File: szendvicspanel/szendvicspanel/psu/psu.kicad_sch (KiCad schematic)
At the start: 7 parts

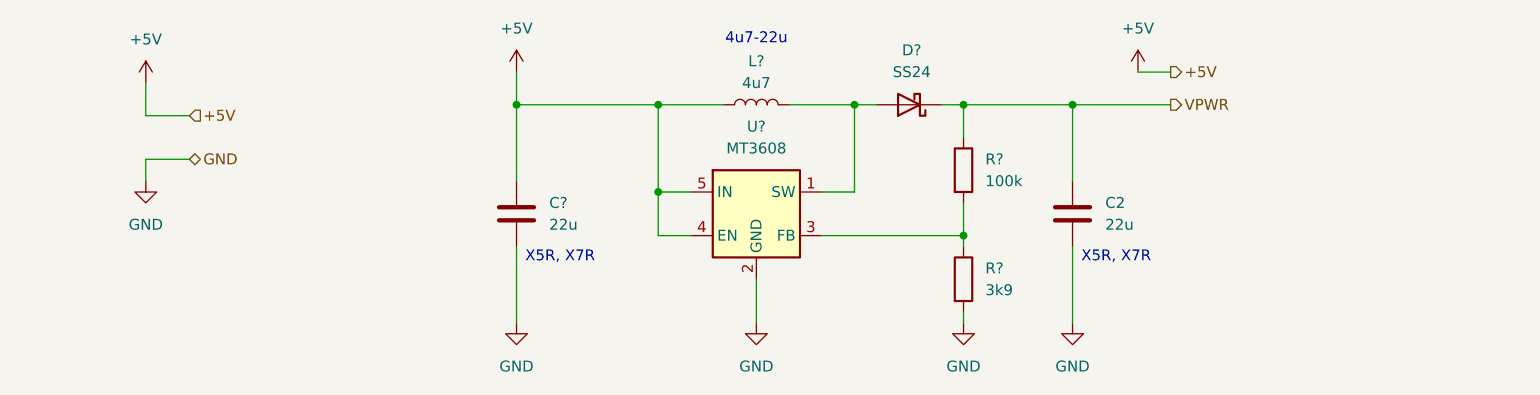
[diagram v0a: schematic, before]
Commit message: Átstrukturálás hierarchikus PCB-hez
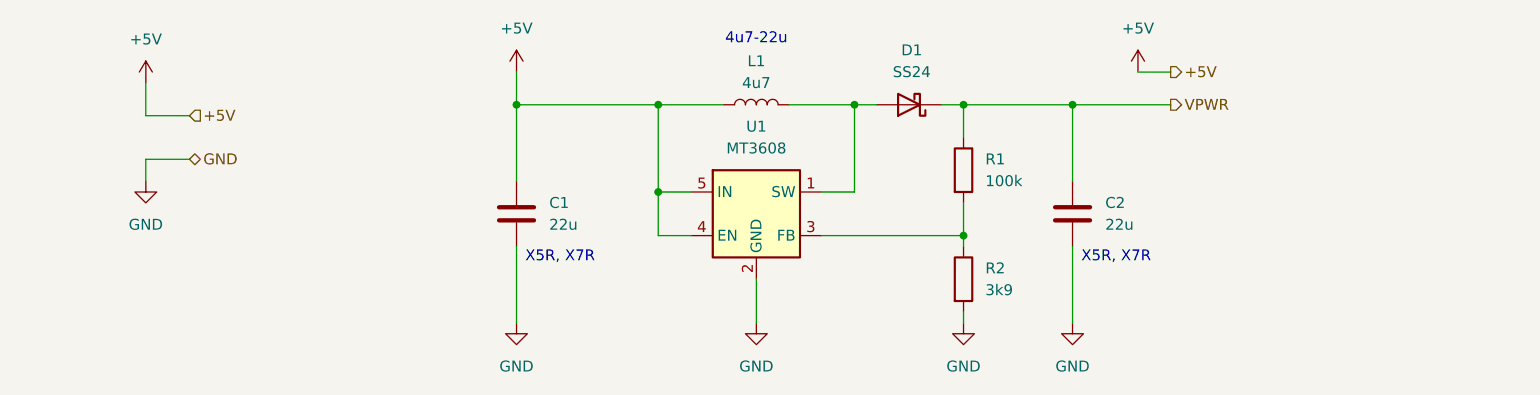
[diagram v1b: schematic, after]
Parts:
- gave numbers to parts that had none: 6
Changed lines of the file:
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@@
 		(dnp no)
 		(fields_autoplaced yes)
-		(property "Reference" "D?"
+		(property "Reference" "D1"
 			(at 167.9575 81.28 0)
 			(effects
@@
 			(project "szendvicspanel"
 				(path "/2e536be4-7a69-4064-ab31-c73232c2dcfe/c1a87f4a-0473-4080-9ef3-9f191c8d170d"
-					(reference "D?")
+					(reference "D1")
 					(unit 1)
 				)
@@
 		(dnp no)
 		(fields_autoplaced yes)
-		(property "Reference" "#PWR?"
+		(property "Reference" "#PWR07"
 			(at 121.92 119.38 0)
 			(effects
@@
 			(project "szendvicspanel"
 				(path "/2e536be4-7a69-4064-ab31-c73232c2dcfe/c1a87f4a-0473-4080-9ef3-9f191c8d170d"
-					(reference "#PWR?")
+					(reference "#PWR07")
 					(unit 1)
 				)
@@
 		(dnp no)
 		(fields_autoplaced yes)
-		(property "Reference" "#PWR015"
+		(property "Reference" "#PWR04"
 			(at 78.74 88.9 0)
 			(effects
@@
 			(project ""
 				(path "/2e536be4-7a69-4064-ab31-c73232c2dcfe/c1a87f4a-0473-4080-9ef3-9f191c8d170d"
-					(reference "#PWR015")
+					(reference "#PWR04")
 					(unit 1)
 				)
@@
 		(dnp no)
 		(fields_autoplaced yes)
-		(property "Reference" "U?"
+		(property "Reference" "U1"
 			(at 149.86 90.17 0)
 			(effects
@@
 			(project "szendvicspanel"
 				(path "/2e536be4-7a69-4064-ab31-c73232c2dcfe/c1a87f4a-0473-4080-9ef3-9f191c8d170d"
-					(reference "U?")
+					(reference "U1")
 					(unit 1)
 				)
@@
 		(dnp no)
 		(fields_autoplaced yes)
-		(property "Reference" "R?"
+		(property "Reference" "R2"
 			(at 176.53 106.6799 0)
 			(effects
@@
 			(project "szendvicspanel"
 				(path "/2e536be4-7a69-4064-ab31-c73232c2dcfe/c1a87f4a-0473-4080-9ef3-9f191c8d170d"
-					(reference "R?")
+					(reference "R2")
 					(unit 1)
 				)
@@
 		(dnp no)
 		(fields_autoplaced yes)
-		(property "Reference" "#PWR?"
+		(property "Reference" "#PWR011"
 			(at 194.31 87.63 0)
 			(effects
@@
 			(project "szendvicspanel"
 				(path "/2e536be4-7a69-4064-ab31-c73232c2dcfe/c1a87f4a-0473-4080-9ef3-9f191c8d170d"
-					(reference "#PWR?")
+					(reference "#PWR011")
 					(unit 1)
 				)
@@
 		(dnp no)
 		(fields_autoplaced yes)
-		(property "Reference" "#PWR?"
+		(property "Reference" "#PWR06"
 			(at 121.92 87.63 0)
 			(effects
@@
 			(project "szendvicspanel"
 				(path "/2e536be4-7a69-4064-ab31-c73232c2dcfe/c1a87f4a-0473-4080-9ef3-9f191c8d170d"
-					(reference "#PWR?")
+					(reference "#PWR06")
 					(unit 1)
 				)
@@
 		(dnp no)
 		(fields_autoplaced yes)
-		(property "Reference" "#PWR?"
+		(property "Reference" "#PWR08"
 			(at 149.86 119.38 0)
 			(effects
@@
 			(project "szendvicspanel"
 				(path "/2e536be4-7a69-4064-ab31-c73232c2dcfe/c1a87f4a-0473-4080-9ef3-9f191c8d170d"
-					(reference "#PWR?")
+					(reference "#PWR08")
 					(unit 1)
 				)
@@
 		(dnp no)
 		(fields_autoplaced yes)
-		(property "Reference" "L?"
+		(property "Reference" "L1"
 			(at 149.86 82.55 90)
 			(effects
@@
 			(project "szendvicspanel"
 				(path "/2e536be4-7a69-4064-ab31-c73232c2dcfe/c1a87f4a-0473-4080-9ef3-9f191c8d170d"
-					(reference "L?")
+					(reference "L1")
 					(unit 1)
 				)
@@
 		(dnp no)
 		(fields_autoplaced yes)
-		(property "Reference" "#PWR?"
+		(property "Reference" "#PWR010"
 			(at 186.69 119.38 0)
 			(effects
@@
 			(project "szendvicspanel"
 				(path "/2e536be4-7a69-4064-ab31-c73232c2dcfe/c1a87f4a-0473-4080-9ef3-9f191c8d170d"
-					(reference "#PWR?")
+					(reference "#PWR010")
 					(unit 1)
 				)
@@
 		(dnp no)
 		(fields_autoplaced yes)
-		(property "Reference" "C?"
+		(property "Reference" "C1"
 			(at 125.73 99.0599 0)
 			(effects
@@
 			(project "szendvicspanel"
 				(path "/2e536be4-7a69-4064-ab31-c73232c2dcfe/c1a87f4a-0473-4080-9ef3-9f191c8d170d"
-					(reference "C?")
+					(reference "C1")
 					(unit 1)
 				)
@@
 		(dnp no)
 		(fields_autoplaced yes)
-		(property "Reference" "#PWR?"
+		(property "Reference" "#PWR09"
 			(at 173.99 119.38 0)
 			(effects
@@
 			(project "szendvicspanel"
 				(path "/2e536be4-7a69-4064-ab31-c73232c2dcfe/c1a87f4a-0473-4080-9ef3-9f191c8d170d"
-					(reference "#PWR?")
+					(reference "#PWR09")
 					(unit 1)
 				)
@@
 		(dnp no)
 		(fields_autoplaced yes)
-		(property "Reference" "R?"
+		(property "Reference" "R1"
 			(at 176.53 93.9799 0)
 			(effects
@@
 			(project "szendvicspanel"
 				(path "/2e536be4-7a69-4064-ab31-c73232c2dcfe/c1a87f4a-0473-4080-9ef3-9f191c8d170d"
-					(reference "R?")
+					(reference "R1")
 					(unit 1)
 				)
@@
 		(dnp no)
 		(fields_autoplaced yes)
-		(property "Reference" "#PWR014"
+		(property "Reference" "#PWR05"
 			(at 78.74 102.87 0)
 			(effects
@@
 			(project "szendvicspanel"
 				(path "/2e536be4-7a69-4064-ab31-c73232c2dcfe/c1a87f4a-0473-4080-9ef3-9f191c8d170d"
-					(reference "#PWR014")
-					(unit 1)
-				)
+					(reference "#PWR05")
+					(unit 1)
+				)

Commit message: Add PSU PCB
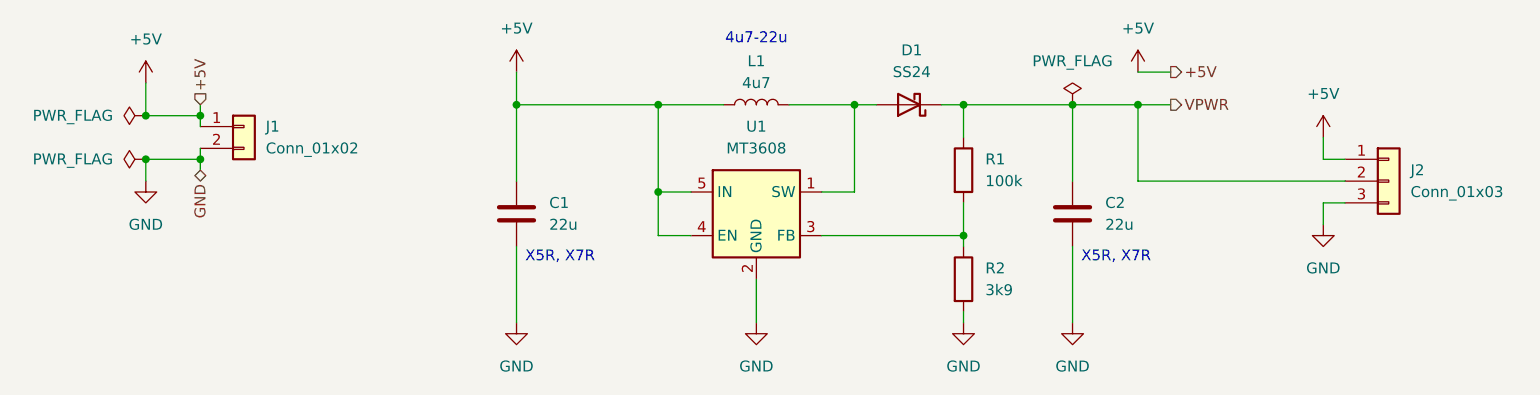
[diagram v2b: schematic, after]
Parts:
- added J1: Conn_01x02, Connector_PinHeader_2.54mm:PinHeader_1x02_P2.54mm_Horizontal, symbol Connector_Generic:Conn_01x02
- added J2: Conn_01x03, Connector_PinHeader_2.54mm:PinHeader_1x03_P2.54mm_Horizontal, symbol Connector_Generic:Conn_01x03
- C1, C2: footprint (none) -> Capacitor_SMD:C_0805_2012Metric_Pad1.18x1.45mm_HandSolder
- L1: footprint (none) -> Inductor_SMD:L_10.4x10.4_H4.8
- R1, R2: footprint (none) -> Resistor_SMD:R_0805_2012Metric_Pad1.20x1.40mm_HandSolder
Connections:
- net +5V: now also J1.1 (Pin_1), J2.1 (Pin_1)
- net GND: now also J1.2 (Pin_2), J2.3 (Pin_3)
- net VPWR: now also J2.2 (Pin_2)
